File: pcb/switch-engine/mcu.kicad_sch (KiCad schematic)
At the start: 76 parts, among them J10 CORTEX_DEBUG_ETM, J12 CONN_01X03, J13 PMOD_HOST, J26 RJ45, J9 PMOD_HOST, U14 ECS-1612MV-250-CN, U17 AT24MAC402, U29 ADM3101E_QFN, U8 XCKU5P-2FFVB676I, U9 STM32H735-UFBGA176-25

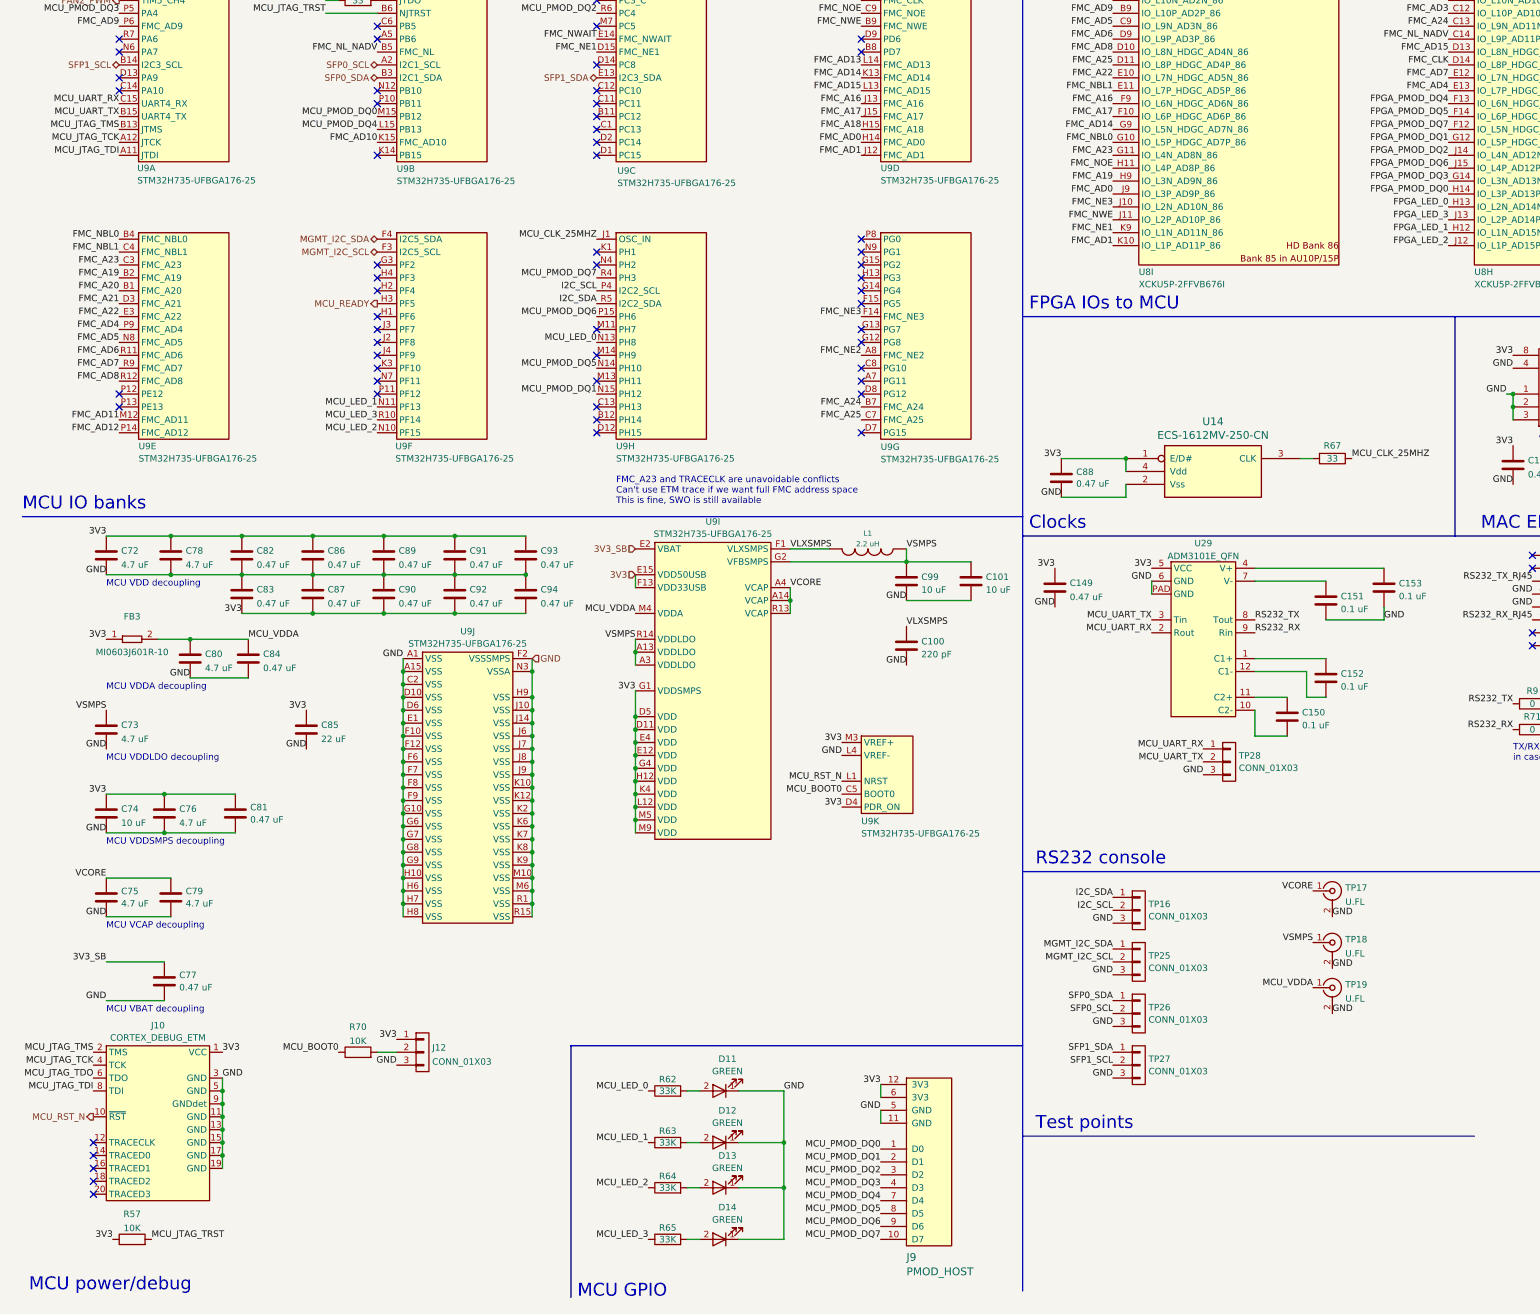
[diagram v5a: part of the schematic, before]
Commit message: Initial power routing of MCU, breakout for FMC signals on FPGA
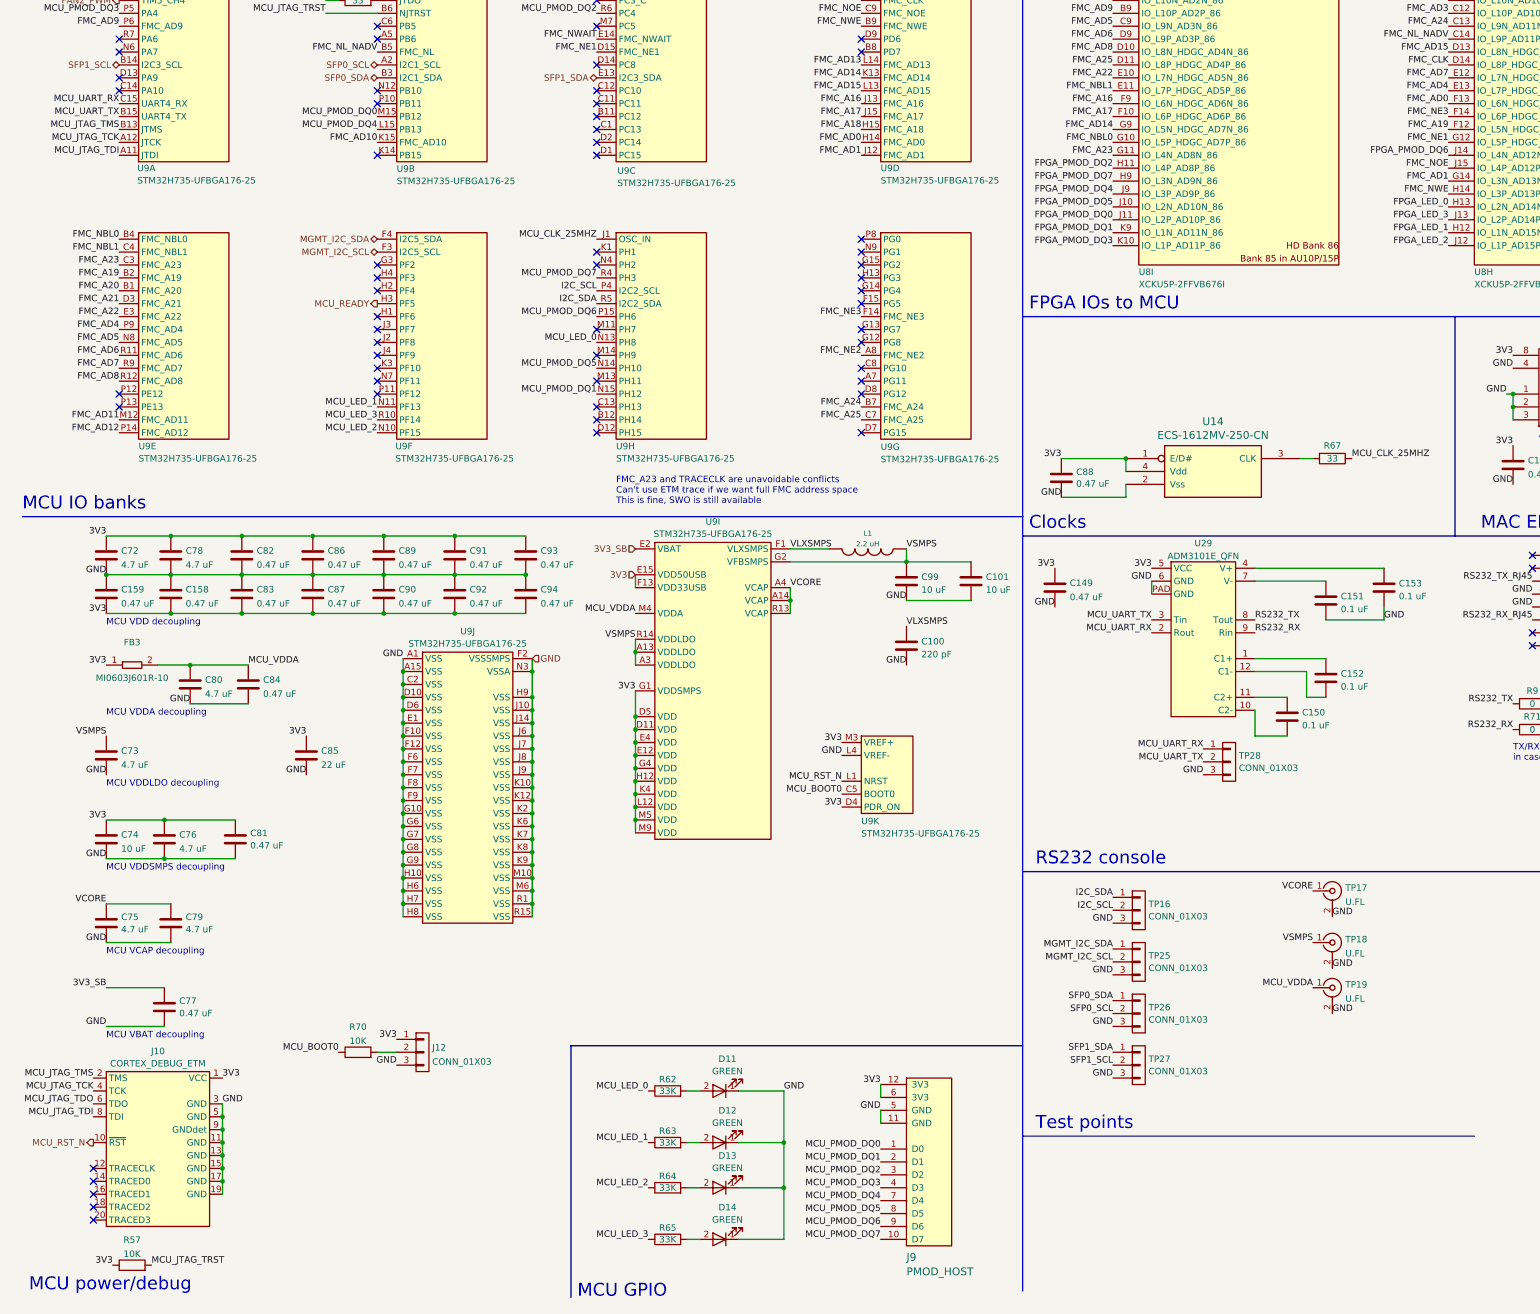
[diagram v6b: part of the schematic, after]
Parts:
- added C158, C159: 0.47 uF, azonenberg_pcb:EIA_0402_CAP_NOSILK, symbol device:C
- C77, C82, C83, C84, C86, C89, C90, C92, C93, C94: footprint azonenberg_pcb:EIA_0402_CAP_NOSILK -> azonenberg_pcb:EIA_0201_CAP_NOSILK
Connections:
- net 3V3: now also C158.2, C159.2
- net FMC_A19: now also U8.F12 (IO_L5N_HDGC_87); no longer U8.H9 (IO_L3N_AD9N_86)
- net FMC_AD0: now also U8.F13 (IO_L6N_HDGC_87); no longer U8.J9 (IO_L3P_AD9P_86)
- net FMC_AD1: now also U8.G14 (IO_L3N_AD13N_87); no longer U8.K10 (IO_L1P_AD11P_86)
- net FMC_NE1: now also U8.G12 (IO_L5P_HDGC_87); no longer U8.K9 (IO_L1N_AD11N_86)
- net FMC_NE3: now also U8.F14 (IO_L6P_HDGC_87); no longer U8.J10 (IO_L2N_AD10N_86)
- net FMC_NOE: now also U8.J15 (IO_L4P_AD12P_87); no longer U8.H11 (IO_L4P_AD8P_86)
- net FMC_NWE: now also U8.H14 (IO_L3P_AD13P_87); no longer U8.J11 (IO_L2P_AD10P_86)
- net FPGA_PMOD_DQ0: now also U8.J11 (IO_L2P_AD10P_86); no longer U8.H14 (IO_L3P_AD13P_87)
- net FPGA_PMOD_DQ1: now also U8.K9 (IO_L1N_AD11N_86); no longer U8.G12 (IO_L5P_HDGC_87)
- net FPGA_PMOD_DQ2: now also U8.H11 (IO_L4P_AD8P_86); no longer U8.J14 (IO_L4N_AD12N_87)
- net FPGA_PMOD_DQ3: now also U8.K10 (IO_L1P_AD11P_86); no longer U8.G14 (IO_L3N_AD13N_87)
- net FPGA_PMOD_DQ4: now also U8.J9 (IO_L3P_AD9P_86); no longer U8.F13 (IO_L6N_HDGC_87)
- net FPGA_PMOD_DQ5: now also U8.J10 (IO_L2N_AD10N_86); no longer U8.F14 (IO_L6P_HDGC_87)
- net FPGA_PMOD_DQ6: now also U8.J14 (IO_L4N_AD12N_87); no longer U8.J15 (IO_L4P_AD12P_87)
- net FPGA_PMOD_DQ7: now also U8.H9 (IO_L3N_AD9N_86); no longer U8.F12 (IO_L5N_HDGC_87)
- net GND: now also C158.1, C159.1
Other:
- moved on the sheet: C73, C74, C75, C76, C77, C79, C80, C81, C84, C85, FB3, J10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

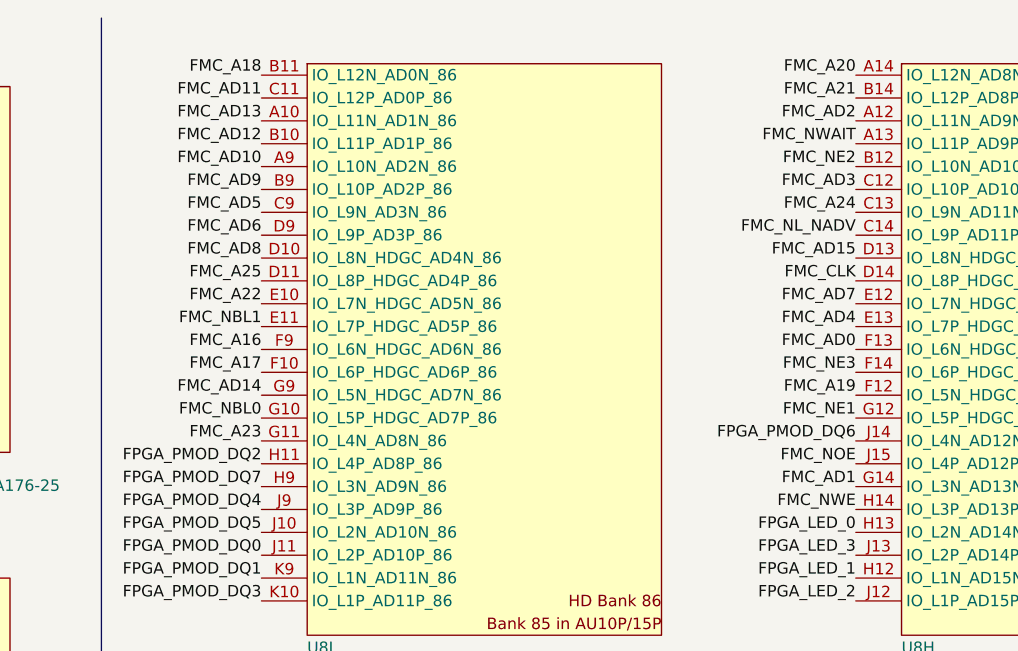
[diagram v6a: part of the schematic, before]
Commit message: Initial routing progress on RGMII and FMC
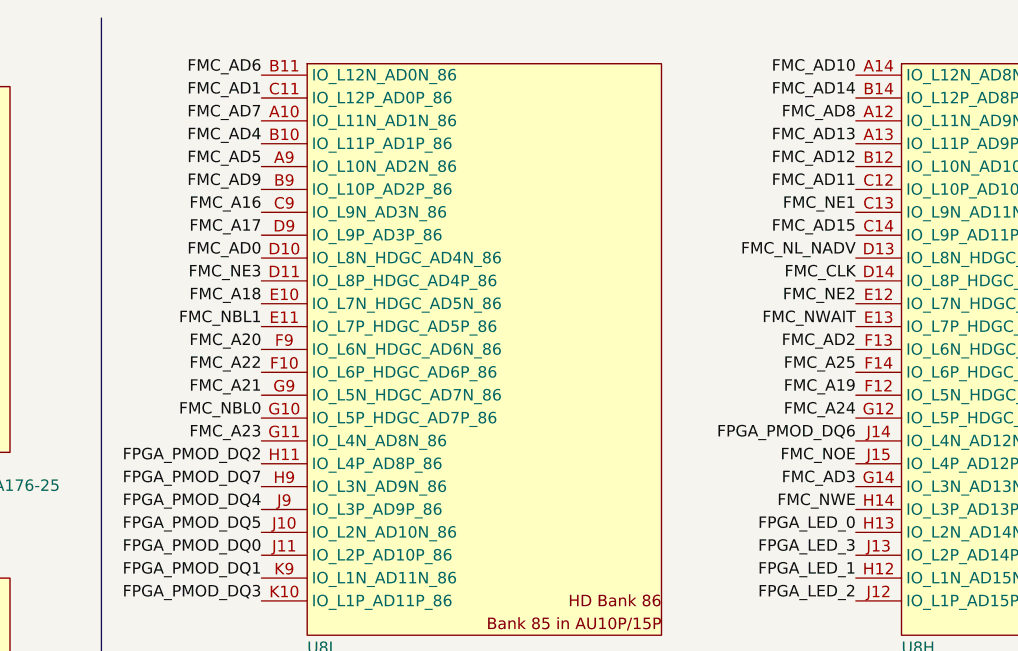
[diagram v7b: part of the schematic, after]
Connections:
- net FMC_A16: now also U8.C9 (IO_L9N_AD3N_86); no longer U8.F9 (IO_L6N_HDGC_AD6N_86)
- net FMC_A17: now also U8.D9 (IO_L9P_AD3P_86); no longer U8.F10 (IO_L6P_HDGC_AD6P_86)
- net FMC_A18: now also U8.E10 (IO_L7N_HDGC_AD5N_86); no longer U8.B11 (IO_L12N_AD0N_86)
- net FMC_A20: now also U8.F9 (IO_L6N_HDGC_AD6N_86); no longer U8.A14 (IO_L12N_AD8N_87)
- net FMC_A21: now also U8.G9 (IO_L5N_HDGC_AD7N_86); no longer U8.B14 (IO_L12P_AD8P_87)
- net FMC_A22: now also U8.F10 (IO_L6P_HDGC_AD6P_86); no longer U8.E10 (IO_L7N_HDGC_AD5N_86)
- net FMC_A24: now also U8.G12 (IO_L5P_HDGC_87); no longer U8.C13 (IO_L9N_AD11N_87)
- net FMC_A25: now also U8.F14 (IO_L6P_HDGC_87); no longer U8.D11 (IO_L8P_HDGC_AD4P_86)
- net FMC_AD0: now also U8.D10 (IO_L8N_HDGC_AD4N_86); no longer U8.F13 (IO_L6N_HDGC_87)
- net FMC_AD1: now also U8.C11 (IO_L12P_AD0P_86); no longer U8.G14 (IO_L3N_AD13N_87)
- net FMC_AD10: now also U8.A14 (IO_L12N_AD8N_87); no longer U8.A9 (IO_L10N_AD2N_86)
- net FMC_AD11: now also U8.C12 (IO_L10P_AD10P_87); no longer U8.C11 (IO_L12P_AD0P_86)
- net FMC_AD12: now also U8.B12 (IO_L10N_AD10N_87); no longer U8.B10 (IO_L11P_AD1P_86)
- net FMC_AD13: now also U8.A13 (IO_L11P_AD9P_87); no longer U8.A10 (IO_L11N_AD1N_86)
- net FMC_AD14: now also U8.B14 (IO_L12P_AD8P_87); no longer U8.G9 (IO_L5N_HDGC_AD7N_86)
- net FMC_AD15: now also U8.C14 (IO_L9P_AD11P_87); no longer U8.D13 (IO_L8N_HDGC_87)
- net FMC_AD2: now also U8.F13 (IO_L6N_HDGC_87); no longer U8.A12 (IO_L11N_AD9N_87)
- net FMC_AD3: now also U8.G14 (IO_L3N_AD13N_87); no longer U8.C12 (IO_L10P_AD10P_87)
- net FMC_AD4: now also U8.B10 (IO_L11P_AD1P_86); no longer U8.E13 (IO_L7P_HDGC_87)
- net FMC_AD5: now also U8.A9 (IO_L10N_AD2N_86); no longer U8.C9 (IO_L9N_AD3N_86)
- net FMC_AD6: now also U8.B11 (IO_L12N_AD0N_86); no longer U8.D9 (IO_L9P_AD3P_86)
- net FMC_AD7: now also U8.A10 (IO_L11N_AD1N_86); no longer U8.E12 (IO_L7N_HDGC_87)
- net FMC_AD8: now also U8.A12 (IO_L11N_AD9N_87); no longer U8.D10 (IO_L8N_HDGC_AD4N_86)
- net FMC_NE1: now also U8.C13 (IO_L9N_AD11N_87); no longer U8.G12 (IO_L5P_HDGC_87)
- net FMC_NE2: now also U8.E12 (IO_L7N_HDGC_87); no longer U8.B12 (IO_L10N_AD10N_87)
- net FMC_NE3: now also U8.D11 (IO_L8P_HDGC_AD4P_86); no longer U8.F14 (IO_L6P_HDGC_87)
- net FMC_NL_NADV: now also U8.D13 (IO_L8N_HDGC_87); no longer U8.C14 (IO_L9P_AD11P_87)
- net FMC_NWAIT: now also U8.E13 (IO_L7P_HDGC_87); no longer U8.A13 (IO_L11P_AD9P_87)
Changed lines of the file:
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@@
 	(title_block
 		(title "LATENTRED Ethernet Switch - Main Board")
-		(date "2025-06-02")
+		(date "2025-06-04")
 		(rev "0.1")
 		(company "Antikernel Labs")
@@
 	)
 	(label "FMC_AD3"
-		(at 294.64 31.75 180)
+		(at 294.64 64.77 180)
 		(fields_autoplaced yes)
 		(effects
@@
 	)
 	(label "FMC_A25"
-		(at 228.6 41.91 180)
+		(at 294.64 52.07 180)
 		(fields_autoplaced yes)
 		(effects
@@
 	)
 	(label "FMC_A18"
-		(at 228.6 19.05 180)
+		(at 228.6 44.45 180)
 		(fields_autoplaced yes)
 		(effects
@@
 	)
 	(label "FMC_NE3"
-		(at 294.64 52.07 180)
+		(at 228.6 41.91 180)
 		(fields_autoplaced yes)
 		(effects
@@
 	)
 	(label "FMC_AD11"
-		(at 228.6 21.59 180)
+		(at 294.64 31.75 180)
 		(fields_autoplaced yes)
 		(effects
@@
 	)
 	(label "FMC_NWAIT"
-		(at 294.64 26.67 180)
+		(at 294.64 46.99 180)
 		(fields_autoplaced yes)
 		(effects
@@
 	)
 	(label "FMC_AD1"
-		(at 294.64 64.77 180)
+		(at 228.6 21.59 180)
 		(fields_autoplaced yes)
 		(effects
@@
 	)
 	(label "FMC_A21"
-		(at 294.64 21.59 180)
+		(at 228.6 54.61 180)
 		(fields_autoplaced yes)
 		(effects
@@
 	)
 	(label "FMC_AD14"
-		(at 228.6 54.61 180)
+		(at 294.64 21.59 180)
 		(fields_autoplaced yes)
 		(effects
@@
 	)
 	(label "FMC_A20"
-		(at 294.64 19.05 180)
+		(at 228.6 49.53 180)
 		(fields_autoplaced yes)
 		(effects
@@
 	)
 	(label "FMC_AD4"
-		(at 294.64 46.99 180)
+		(at 228.6 26.67 180)
 		(fields_autoplaced yes)
 		(effects
@@
 	)
 	(label "FMC_AD6"
-		(at 228.6 36.83 180)
+		(at 228.6 19.05 180)
 		(fields_autoplaced yes)
 		(effects
@@
 	)
 	(label "FMC_AD10"
-		(at 228.6 29.21 180)
+		(at 294.64 19.05 180)
 		(fields_autoplaced yes)
 		(effects
@@
 	)
 	(label "FMC_AD7"
-		(at 294.64 44.45 180)
+		(at 228.6 24.13 180)
 		(fields_autoplaced yes)
 		(effects
@@
 	)
 	(label "FMC_AD2"
-		(at 294.64 24.13 180)
+		(at 294.64 49.53 180)
 		(fields_autoplaced yes)
 		(effects
@@
 	)
 	(label "FMC_A22"
-		(at 228.6 44.45 180)
+		(at 228.6 52.07 180)
 		(fields_autoplaced yes)
 		(effects
@@
 	)
 	(label "FMC_A24"
-		(at 294.64 34.29 180)
+		(at 294.64 57.15 180)
 		(fields_autoplaced yes)
 		(effects
@@
 	)
 	(label "FMC_NL_NADV"
-		(at 294.64 36.83 180)
+		(at 294.64 39.37 180)
 		(fields_autoplaced yes)
 		(effects
@@
 	)
 	(label "FMC_AD13"
-		(at 228.6 24.13 180)
+		(at 294.64 26.67 180)
 		(fields_autoplaced yes)
 		(effects
@@
 	)
 	(label "FMC_A17"
-		(at 228.6 52.07 180)
+		(at 228.6 36.83 180)
 		(fields_autoplaced yes)
 		(effects
@@
 	)
 	(label "FMC_AD5"
-		(at 228.6 34.29 180)
+		(at 228.6 29.21 180)
 		(fields_autoplaced yes)
 		(effects
@@
 	)
 	(label "FMC_AD15"
-		(at 294.64 39.37 180)
+		(at 294.64 36.83 180)
 		(fields_autoplaced yes)
 		(effects
@@
 	)
 	(label "FMC_AD8"
-		(at 228.6 39.37 180)
+		(at 294.64 24.13 180)
 		(fields_autoplaced yes)
 		(effects
@@
 	)
 	(label "FMC_NE1"
-		(at 294.64 57.15 180)
+		(at 294.64 34.29 180)
 		(fields_autoplaced yes)
 		(effects
@@
 	)
 	(label "FMC_AD0"
-		(at 294.64 49.53 180)
+		(at 228.6 39.37 180)
 		(fields_autoplaced yes)
 		(effects
@@
 	)
 	(label "FMC_AD12"
-		(at 228.6 26.67 180)
+		(at 294.64 29.21 180)
 		(fields_autoplaced yes)
 		(effects
@@
 	)
 	(label "FMC_A16"
-		(at 228.6 49.53 180)
+		(at 228.6 34.29 180)
 		(fields_autoplaced yes)
 		(effects
@@
 	)
 	(label "FMC_NE2"
-		(at 294.64 29.21 180)
+		(at 294.64 44.45 180)
 		(fields_autoplaced yes)
 		(effects
